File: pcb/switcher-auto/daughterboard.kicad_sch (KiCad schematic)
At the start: 71 parts, among them J0 MD-90SM, J5 Conn_02x22_Top_Bottom

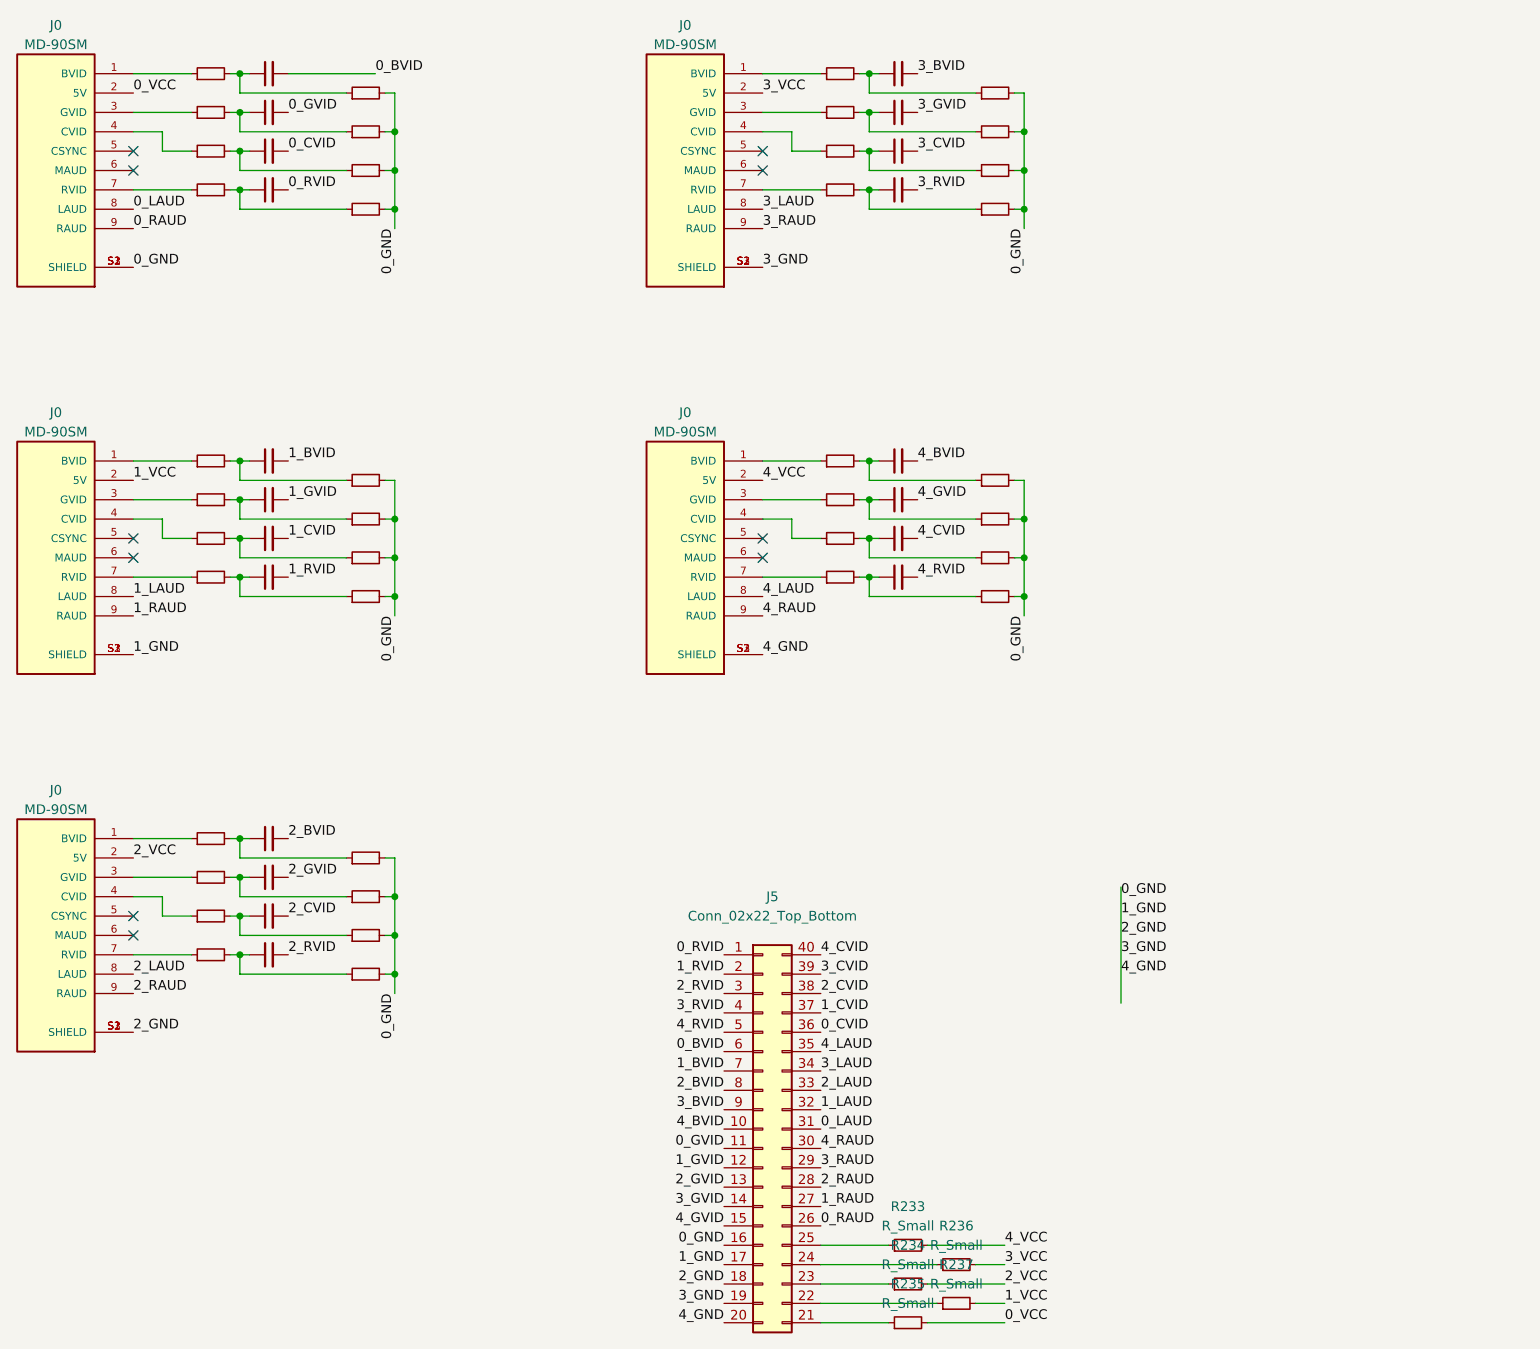
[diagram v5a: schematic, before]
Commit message: WIP dual supply audio switching
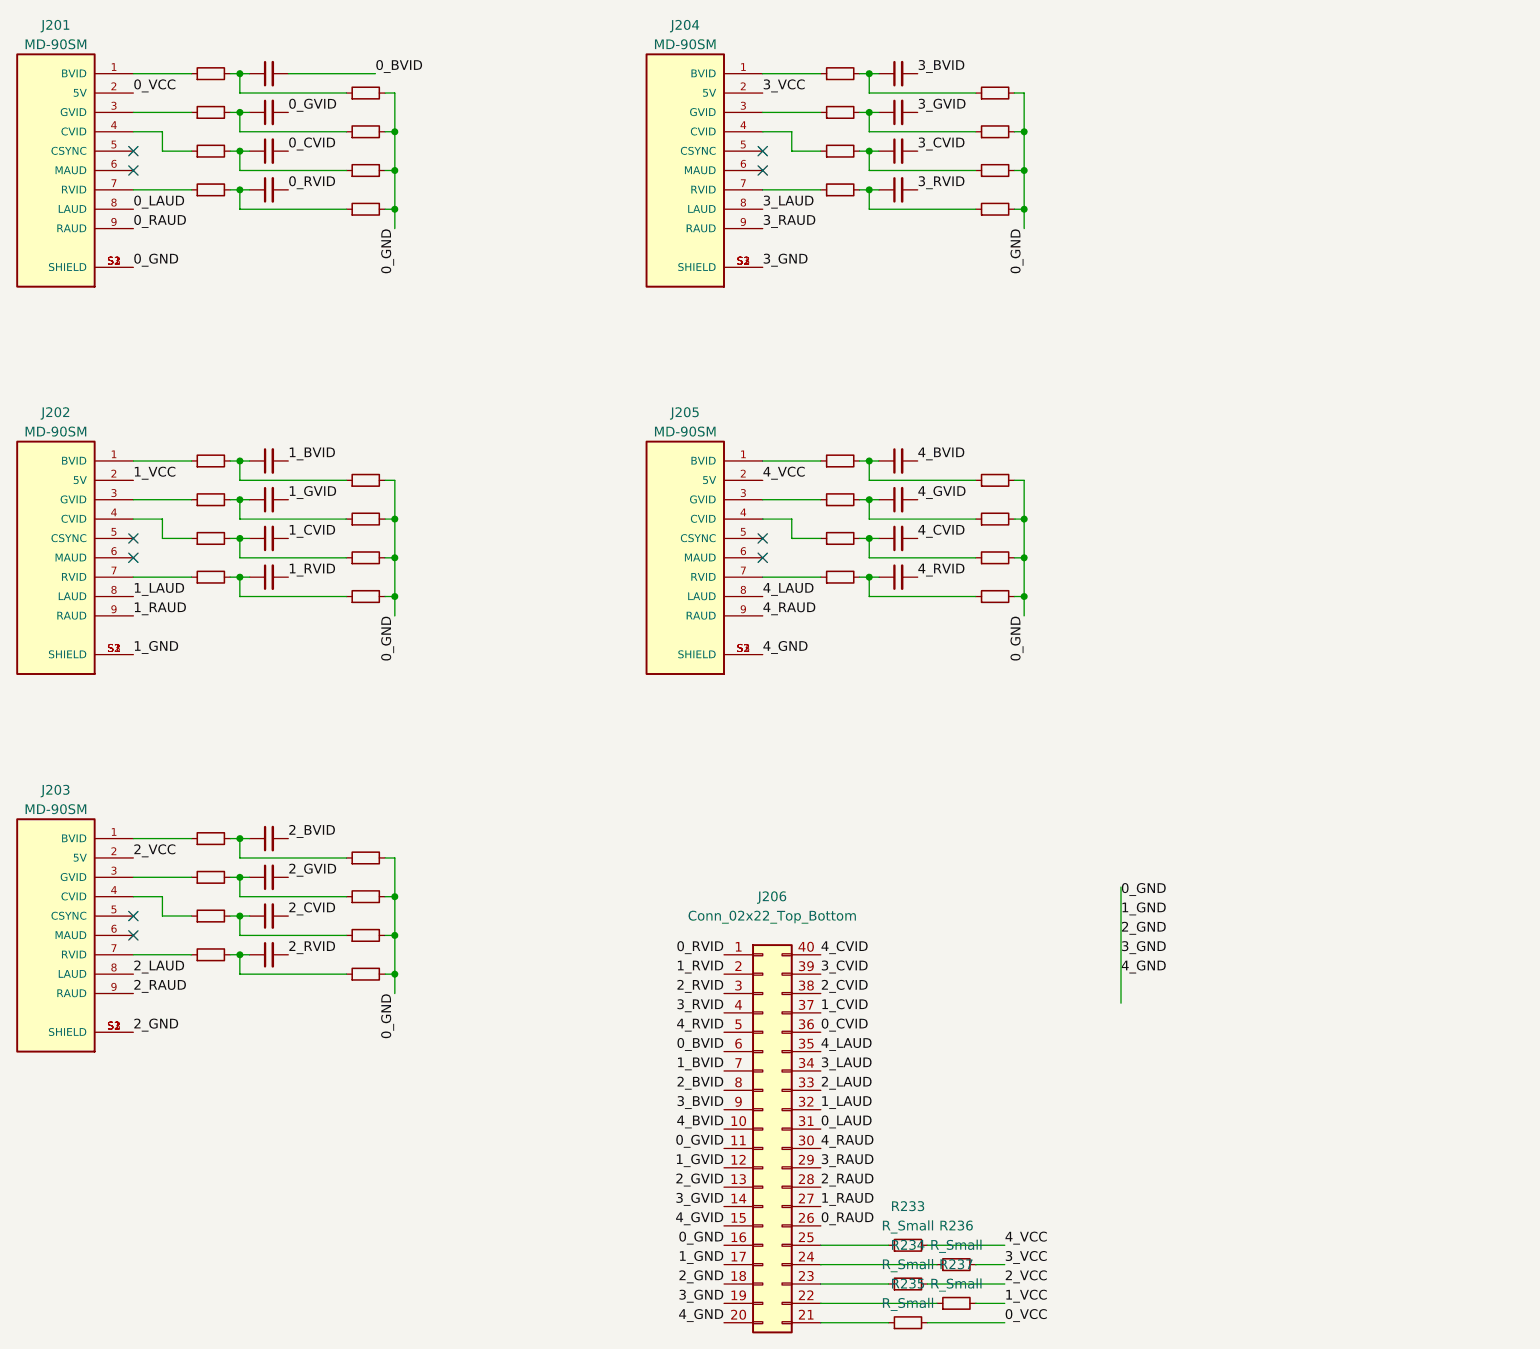
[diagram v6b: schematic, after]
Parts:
- renumbered J0 to J201, J0 to J202, J0 to J203, J0 to J204, J0 to J205, J5 to J206

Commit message: Rev3
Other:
- company: (none) -> @partlyhuman
- title: (none) -> OveRGBkill
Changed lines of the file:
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@@
 	(generator "eeschema")
 	(generator_version "9.0")
-	(paper "A4")
+	(paper "A3")
+	(title_block
+		(title "OveRGBkill")
+		(date "2026-02-28")
+		(rev "3")
+		(company "@partlyhuman")
+	)
 	(junction
 		(at 71.12 31.75)
